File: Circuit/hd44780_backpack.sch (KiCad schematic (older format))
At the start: 20 parts, among them IC1 ATTINY84A-SS, P1 I2C, P10 GND, P2 ISCP, P3 A0, P4 A1, P5 A7, P6 8, P7 10, P8 SERIAL QA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

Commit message: non-working circuit.
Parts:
- removed P10: GND, symbol CONN_1
- removed P3: A0, symbol CONN_1
- removed P4: A1, symbol CONN_1
- removed P5: A7, symbol CONN_1
- removed P6: 8, symbol CONN_1
- removed P7: 10, symbol CONN_1
- removed P8: SERIAL QA, symbol CONN_1
- removed P9: +5V, symbol CONN_1
- added M1: MESHTHING, MeshThing, symbol MESHTHING
- added P3: ATTINY_BREAKOUT, symbol ATTINY_BREAKOUT
- added P4: POWER, symbol CONN_2
- added P5, P6: CONN_10, symbol CONN_10
- added P7: CONN_4, symbol CONN_4
- added P8: CONN_4X2, symbol CONN_4X2
- added R3: 10k, ~, symbol R
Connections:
- wire segments 95 -> 169
- no-connect marks 0 -> 7
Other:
- moved on the sheet: 10k1, C1, C2, IC1, P1, P2, Q1, R1, R2, SW1, U2

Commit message: Meshthing integration complete
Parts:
- removed P4: POWER, symbol CONN_2
- added K1: PWR_SHIFT, symbol CONN_3
- added P4: USB_5PIN_SHELL, ~, symbol USB_5PIN_SHELL
- added P9: CONN_2, symbol CONN_2
- added Q2, Q3: BSS138, SOT23, symbol BSS138
- added R4, R5, R6, R7: 10K, ~, symbol R
- added R8: 1K, ~, symbol R
- added R9: 2.2K, ~, symbol R
- P5: value CONN_10 -> MESH_BKOUT_1-10
- P6: value CONN_10 -> MESH_BKOUT_11-20
- P7: value CONN_4 -> MESH_ENABLE
- P8: value CONN_4X2 -> ATTINY_ENABLE
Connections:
- net labels added: +3.3V
- wire segments 169 -> 182
- no-connect marks 7 -> 10
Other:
- moved on the sheet: P1

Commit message: Changed to using a BSS138DW
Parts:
- removed Q2, Q3: BSS138, SOT23, symbol BSS138
- added Q2: BSS138DW, SOT-23, symbol BSS138DW
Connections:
- wire segments 182 -> 183
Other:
- moved on the sheet: R6, R7

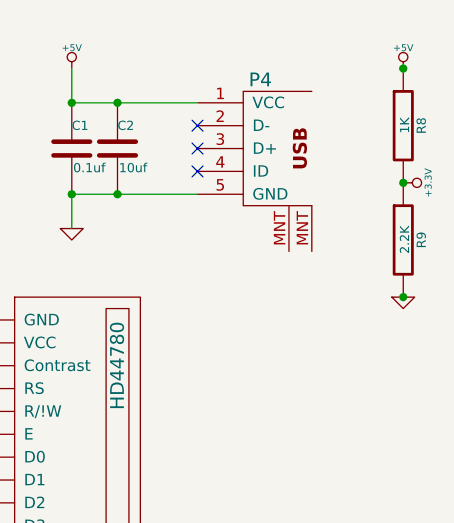
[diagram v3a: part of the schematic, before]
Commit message: problem with back masks
the meshthingy had no back mask area.  made it very difficult to solder.
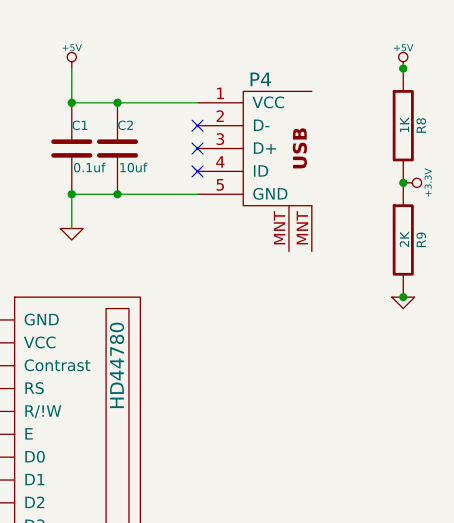
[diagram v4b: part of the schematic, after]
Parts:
- R9: value 2.2K -> 2K
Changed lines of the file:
@@
 Sheet 1 1
 Title ""
-Date "4 jun 2014"
+Date "23 jun 2014"
 Rev ""
 Comp ""
@@
 P 9800 1700
 F 0 "R9" V 9880 1700 40  0000 C CNN
-F 1 "2.2K" V 9807 1701 40  0000 C CNN
+F 1 "2K" V 9807 1701 40  0000 C CNN
 F 2 "~" V 9730 1700 30  0000 C CNN
 F 3 "~" H 9800 1700 30  0000 C CNN
